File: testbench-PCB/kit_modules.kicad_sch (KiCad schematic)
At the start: 14 parts, among them U2 Rotary_encoder_switch_module, U3 Thermistor_module, U4 Relay_module, U6 Matrix_keyboard, U7 RTC_EEPROM_module, U8 LCD_display

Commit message: Updated footprints, PCB.
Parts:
- U2: footprint Connector_PinSocket_2.54mm:PinSocket_1x05_P2.54mm_Horizontal -> kit_modules:Encoder_module
- U4: footprint (none) -> kit_modules:Relay_module
- U7: footprint Connector_PinSocket_2.54mm:PinSocket_1x06_P2.54mm_Horizontal -> Connector_PinSocket_2.54mm:PinSocket_1x06_P2.54mm_Vertical
- U8: footprint (none) -> kit_modules:LCD_1602A_module
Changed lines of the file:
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@@
       (effects (font (size 1.27 1.27)))
     )
-    (property "Footprint" "" (at 177.8 54.61 0)
+    (property "Footprint" "kit_modules:Relay_module" (at 177.8 54.61 0)
       (effects (font (size 1.27 1.27)) hide)
     )
@@
       (effects (font (size 1.27 1.27)))
     )
-    (property "Footprint" "" (at 179.07 151.13 0)
+    (property "Footprint" "kit_modules:LCD_1602A_module" (at 179.07 151.13 0)
       (effects (font (size 1.27 1.27)) hide)
     )
@@
       (effects (font (size 1.27 1.27)))
     )
-    (property "Footprint" "Connector_PinSocket_2.54mm:PinSocket_1x05_P2.54mm_Horizontal" (at 87.63 50.8 0)
+    (property "Footprint" "kit_modules:Encoder_module" (at 87.63 50.8 0)
       (effects (font (size 1.27 1.27)) hide)
     )
@@
       (effects (font (size 1.27 1.27)))
     )
-    (property "Footprint" "Connector_PinSocket_2.54mm:PinSocket_1x06_P2.54mm_Horizontal" (at 90.17 177.8 0)
-      (effects (font (size 1.27 1.27)) hide)
-    )
+    (property "Footprint" "Connector_PinSocket_2.54mm:PinSocket_1x06_P2.54mm_Vertical" (at 90.17 177.8 0)
+      (effects (font (size 1.27 1.27)) hide)
+    )

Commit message: Routed osc., USB interface.
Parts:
- U3: footprint Connector_PinSocket_2.54mm:PinSocket_1x04_P2.54mm_Horizontal -> Connector_PinSocket_2.54mm:PinSocket_1x04_P2.54mm_Vertical
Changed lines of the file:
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@@
       (effects (font (size 1.27 1.27)))
     )
-    (property "Footprint" "Connector_PinSocket_2.54mm:PinSocket_1x04_P2.54mm_Horizontal" (at 210.82 95.25 0)
+    (property "Footprint" "Connector_PinSocket_2.54mm:PinSocket_1x04_P2.54mm_Vertical" (at 210.82 95.25 0)
       (effects (font (size 1.27 1.27)) hide)
     )

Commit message: Fixed footprints in schematics.
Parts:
- U2: footprint kit_modules:Encoder_module -> kit_modules:Rotary_encoder_module
- U3: footprint Connector_PinSocket_2.54mm:PinSocket_1x04_P2.54mm_Vertical -> kit_modules:Thermistor_module
- U7: footprint Connector_PinSocket_2.54mm:PinSocket_1x06_P2.54mm_Vertical -> kit_modules:RTC_module
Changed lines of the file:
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@@
       (effects (font (size 1.27 1.27)))
     )
-    (property "Footprint" "Connector_PinSocket_2.54mm:PinSocket_1x04_P2.54mm_Vertical" (at 210.82 95.25 0)
+    (property "Footprint" "kit_modules:Thermistor_module" (at 210.82 95.25 0)
       (effects (font (size 1.27 1.27)) hide)
     )
@@
       (effects (font (size 1.27 1.27)))
     )
-    (property "Footprint" "kit_modules:Encoder_module" (at 87.63 50.8 0)
+    (property "Footprint" "kit_modules:Rotary_encoder_module" (at 87.63 50.8 0)
       (effects (font (size 1.27 1.27)) hide)
     )
@@
       (effects (font (size 1.27 1.27)))
     )
-    (property "Footprint" "Connector_PinSocket_2.54mm:PinSocket_1x06_P2.54mm_Vertical" (at 90.17 177.8 0)
+    (property "Footprint" "kit_modules:RTC_module" (at 90.17 177.8 0)
       (effects (font (size 1.27 1.27)) hide)
     )

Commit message: Routing the PCB.
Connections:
- net +5V: now also U8.19 (5V); no longer U8.8 (5V)
- net GND: now also U8.20 (GND), U8.21 (GND); no longer U8.9 (GND)
- net LCD_AO: now also U8.23 (A0); no longer U8.10 (A0)
- net LCD_D0: now reaches U8.5 (D4)
- net LCD_D1: now reaches U8.6 (D5)
- net LCD_D2: now reaches U8.7 (D6)
- net KEY_D0: now reaches U6.1 (ROW1)
- net KEY_D1: now reaches U6.2 (ROW2)
- net KEY_D2: now reaches U6.3 (ROW3)
- net KEY_D3: now reaches U6.4 (ROW4)
- net KEY_D4: now reaches U6.5 (COL1)
- net KEY_D5: now reaches U6.6 (COL2)
- net KEY_D6: now reaches U6.7 (COL3)
- net KEY_D7: now reaches U6.8 (COL4)
- net A renamed ENC.A
- net B renamed ENC.B
- net SW renamed ENC.SW
- new net LCD_D3: U8.8 (D7)
- new net LCD_D4: U8.9 (RS)
- new net LCD_D5: U8.10 (E)
- new net LCD_D6: U8.17 (RST)

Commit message: Finished PCB routing, added ground plane.
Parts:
- C10: value C -> 1uF; footprint (none) -> Capacitor_SMD:C_0805_2012Metric
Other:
- moved on the sheet: U6
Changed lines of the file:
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@@
     (stroke (width 0) (type default))
   )
-  (bus_entry (at 81.28 105.41) (size 2.54 -2.54)
+  (bus_entry (at 82.55 105.41) (size 2.54 -2.54)
     (stroke (width 0) (type default))
   )
@@
     (stroke (width 0) (type default))
   )
-  (bus_entry (at 96.52 105.41) (size 2.54 -2.54)
+  (bus_entry (at 97.79 105.41) (size 2.54 -2.54)
     (stroke (width 0) (type default))
   )
@@
     (stroke (width 0) (type default))
   )
-  (bus_entry (at 88.9 105.41) (size 2.54 -2.54)
+  (bus_entry (at 90.17 105.41) (size 2.54 -2.54)
     (stroke (width 0) (type default))
   )
@@
     (stroke (width 0) (type default))
   )
-  (bus_entry (at 83.82 105.41) (size 2.54 -2.54)
+  (bus_entry (at 85.09 105.41) (size 2.54 -2.54)
     (stroke (width 0) (type default))
   )
@@
     (stroke (width 0) (type default))
   )
-  (bus_entry (at 86.36 105.41) (size 2.54 -2.54)
+  (bus_entry (at 87.63 105.41) (size 2.54 -2.54)
     (stroke (width 0) (type default))
   )
@@
     (stroke (width 0) (type default))
   )
-  (bus_entry (at 93.98 105.41) (size 2.54 -2.54)
-    (stroke (width 0) (type default))
-  )
-  (bus_entry (at 91.44 105.41) (size 2.54 -2.54)
+  (bus_entry (at 95.25 105.41) (size 2.54 -2.54)
+    (stroke (width 0) (type default))
+  )
+  (bus_entry (at 92.71 105.41) (size 2.54 -2.54)
     (stroke (width 0) (type default))
   )
@@
     (stroke (width 0) (type default))
   )
-  (bus_entry (at 78.74 105.41) (size 2.54 -2.54)
+  (bus_entry (at 80.01 105.41) (size 2.54 -2.54)
     (stroke (width 0) (type default))
   )
@@
     (stroke (width 0) (type default))
   )
-  (bus (pts (xy 62.23 105.41) (xy 78.74 105.41))
+  (bus (pts (xy 62.23 105.41) (xy 80.01 105.41))
     (stroke (width 0) (type default))
   )
@@
     (stroke (width 0) (type default))
   )
-  (wire (pts (xy 81.28 92.075) (xy 81.28 102.87))
+  (wire (pts (xy 82.55 92.71) (xy 82.55 102.87))
     (stroke (width 0) (type default))
   )
@@
     (stroke (width 0) (type default))
   )
-  (bus (pts (xy 78.74 105.41) (xy 81.28 105.41))
-    (stroke (width 0) (type default))
-  )
-  (wire (pts (xy 86.36 92.075) (xy 86.36 102.87))
+  (bus (pts (xy 80.01 105.41) (xy 82.55 105.41))
+    (stroke (width 0) (type default))
+  )
+  (wire (pts (xy 87.63 92.71) (xy 87.63 102.87))
     (stroke (width 0) (type default))
   )
@@
     (stroke (width 0) (type default))
   )
-  (wire (pts (xy 88.9 92.075) (xy 88.9 102.87))
+  (wire (pts (xy 90.17 92.71) (xy 90.17 102.87))
     (stroke (width 0) (type default))
   )
@@
     (stroke (width 0) (type default))
   )
-  (bus (pts (xy 83.82 105.41) (xy 86.36 105.41))
+  (bus (pts (xy 85.09 105.41) (xy 87.63 105.41))
     (stroke (width 0) (type default))
   )
@@
     (stroke (width 0) (type default))
   )
-  (wire (pts (xy 96.52 92.075) (xy 96.52 102.87))
+  (wire (pts (xy 97.79 92.71) (xy 97.79 102.87))
     (stroke (width 0) (type default))
   )
@@
     (stroke (width 0) (type default))
   )
-  (bus (pts (xy 86.36 105.41) (xy 88.9 105.41))
+  (bus (pts (xy 87.63 105.41) (xy 90.17 105.41))
     (stroke (width 0) (type default))
   )
@@
     (stroke (width 0) (type default))
   )
-  (wire (pts (xy 83.82 92.075) (xy 83.82 102.87))
+  (wire (pts (xy 85.09 92.71) (xy 85.09 102.87))
     (stroke (width 0) (type default))
   )
@@
     (stroke (width 0) (type default))
   )
-  (wire (pts (xy 99.06 92.075) (xy 99.06 102.87))
+  (wire (pts (xy 100.33 92.71) (xy 100.33 102.87))
     (stroke (width 0) (type default))
   )
@@
     (stroke (width 0) (type default))
   )
-  (wire (pts (xy 91.44 92.075) (xy 91.44 102.87))
-    (stroke (width 0) (type default))
-  )
-  (bus (pts (xy 91.44 105.41) (xy 93.98 105.41))
+  (wire (pts (xy 92.71 92.71) (xy 92.71 102.87))
+    (stroke (width 0) (type default))
+  )
+  (bus (pts (xy 92.71 105.41) (xy 95.25 105.41))
     (stroke (width 0) (type default))
   )
@@
     (stroke (width 0) (type default))
   )
-  (wire (pts (xy 93.98 92.075) (xy 93.98 102.87))
+  (wire (pts (xy 95.25 92.71) (xy 95.25 102.87))
     (stroke (width 0) (type default))
   )
@@
     (stroke (width 0) (type default))
   )
-  (bus (pts (xy 88.9 105.41) (xy 91.44 105.41))
-    (stroke (width 0) (type default))
-  )
-  (bus (pts (xy 81.28 105.41) (xy 83.82 105.41))
-    (stroke (width 0) (type default))
-  )
-  (bus (pts (xy 93.98 105.41) (xy 96.52 105.41))
+  (bus (pts (xy 90.17 105.41) (xy 92.71 105.41))
+    (stroke (width 0) (type default))
+  )
+  (bus (pts (xy 82.55 105.41) (xy 85.09 105.41))
+    (stroke (width 0) (type default))
+  )
+  (bus (pts (xy 95.25 105.41) (xy 97.79 105.41))
     (stroke (width 0) (type default))
   )
@@
     (effects (font (size 1.27 1.27)) (justify left bottom))
   )
-  (label "KEY_D3" (at 88.9 102.87 90) (fields_autoplaced)
-    (effects (font (size 1.27 1.27)) (justify left bottom))
-  )
-  (label "KEY_D0" (at 81.28 102.87 90) (fields_autoplaced)
+  (label "KEY_D3" (at 90.17 102.87 90) (fields_autoplaced)
+    (effects (font (size 1.27 1.27)) (justify left bottom))
+  )
+  (label "KEY_D0" (at 82.55 102.87 90) (fields_autoplaced)
     (effects (font (size 1.27 1.27)) (justify left bottom))
   )
@@
     (effects (font (size 1.27 1.27)) (justify left bottom))
   )
-  (label "KEY_D2" (at 86.36 102.87 90) (fields_autoplaced)
+  (label "KEY_D2" (at 87.63 102.87 90) (fields_autoplaced)
     (effects (font (size 1.27 1.27)) (justify left bottom))
   )
@@
     (effects (font (size 1.27 1.27)) (justify left bottom))
   )
-  (label "KEY_D1" (at 83.82 102.87 90) (fields_autoplaced)
+  (label "KEY_D1" (at 85.09 102.87 90) (fields_autoplaced)
     (effects (font (size 1.27 1.27)) (justify left bottom))
   )
@@
     (effects (font (size 1.27 1.27)) (justify right bottom))
   )
-  (label "KEY_D5" (at 93.98 102.87 90) (fields_autoplaced)
-    (effects (font (size 1.27 1.27)) (justify left bottom))
-  )
-  (label "KEY_D4" (at 91.44 102.87 90) (fields_autoplaced)
+  (label "KEY_D5" (at 95.25 102.87 90) (fields_autoplaced)
+    (effects (font (size 1.27 1.27)) (justify left bottom))
+  )
+  (label "KEY_D4" (at 92.71 102.87 90) (fields_autoplaced)
     (effects (font (size 1.27 1.27)) (justify left bottom))
   )
@@
     (effects (font (size 1.27 1.27)) (justify left bottom))
   )
-  (label "KEY_D6" (at 96.52 102.87 90) (fields_autoplaced)
-    (effects (font (size 1.27 1.27)) (justify left bottom))
-  )
-  (label "KEY_D7" (at 99.06 102.87 90) (fields_autoplaced)
+  (label "KEY_D6" (at 97.79 102.87 90) (fields_autoplaced)
+    (effects (font (size 1.27 1.27)) (justify left bottom))
+  )
+  (label "KEY_D7" (at 100.33 102.87 90) (fields_autoplaced)
     (effects (font (size 1.27 1.27)) (justify left bottom))
   )
@@
       (effects (font (size 1.27 1.27)))
     )
-    (property "Value" "C" (at 78.74 123.19 90)
-      (effects (font (size 1.27 1.27)))
-    )
-    (property "Footprint" "" (at 82.55 127.3048 0)
+    (property "Value" "1uF" (at 78.74 123.19 90)
+      (effects (font (size 1.27 1.27)))
+    )
+    (property "Footprint" "Capacitor_SMD:C_0805_2012Metric" (at 82.55 127.3048 0)
       (effects (font (size 1.27 1.27)) hide)
     )
@@
     )
   )
-  (symbol (lib_id "kit_modules:matrix_keyboard") (at 78.74 89.535 0) (unit 1)
+  (symbol (lib_id "kit_modules:matrix_keyboard") (at 80.01 90.17 0) (unit 1)
     (in_bom yes) (on_board yes) (dnp no)
-    (property "Reference" "U6" (at 102.87 81.28 0)
+    (property "Reference" "U6" (at 104.14 81.915 0)
       (effects (font (size 1.27 1.27)) (justify left))
     )
-    (property "Value" "Matrix_keyboard" (at 86.36 71.755 0)
-      (effects (font (size 1.27 1.27)))
-    )
-    (property "Footprint" "Connector_PinSocket_2.54mm:PinSocket_1x08_P2.54mm_Vertical" (at 78.74 89.535 0)
-      (effects (font (size 1.27 1.27)) hide)
-    )
-    (property "Datasheet" "" (at 78.74 89.535 0)
-      (effects (font (size 1.27 1.27)) hide)
-    )
+    (property "Value" "Matrix_keyboard" (at 87.63 72.39 0)
+      (effects (font (size 1.27 1.27)))
+    )
+    (property "Footprint" "Connector_PinSocket_2.54mm:PinSocket_1x08_P2.54mm_Vertical" (at 80.01 90.17 0)
+      (effects (font (size 1.27 1.27)) hide)
+    )
+    (property "Datasheet" "" (at 80.01 90.17 0)
+      (effects (font (size 1.27 1.27)) hide)
+    )

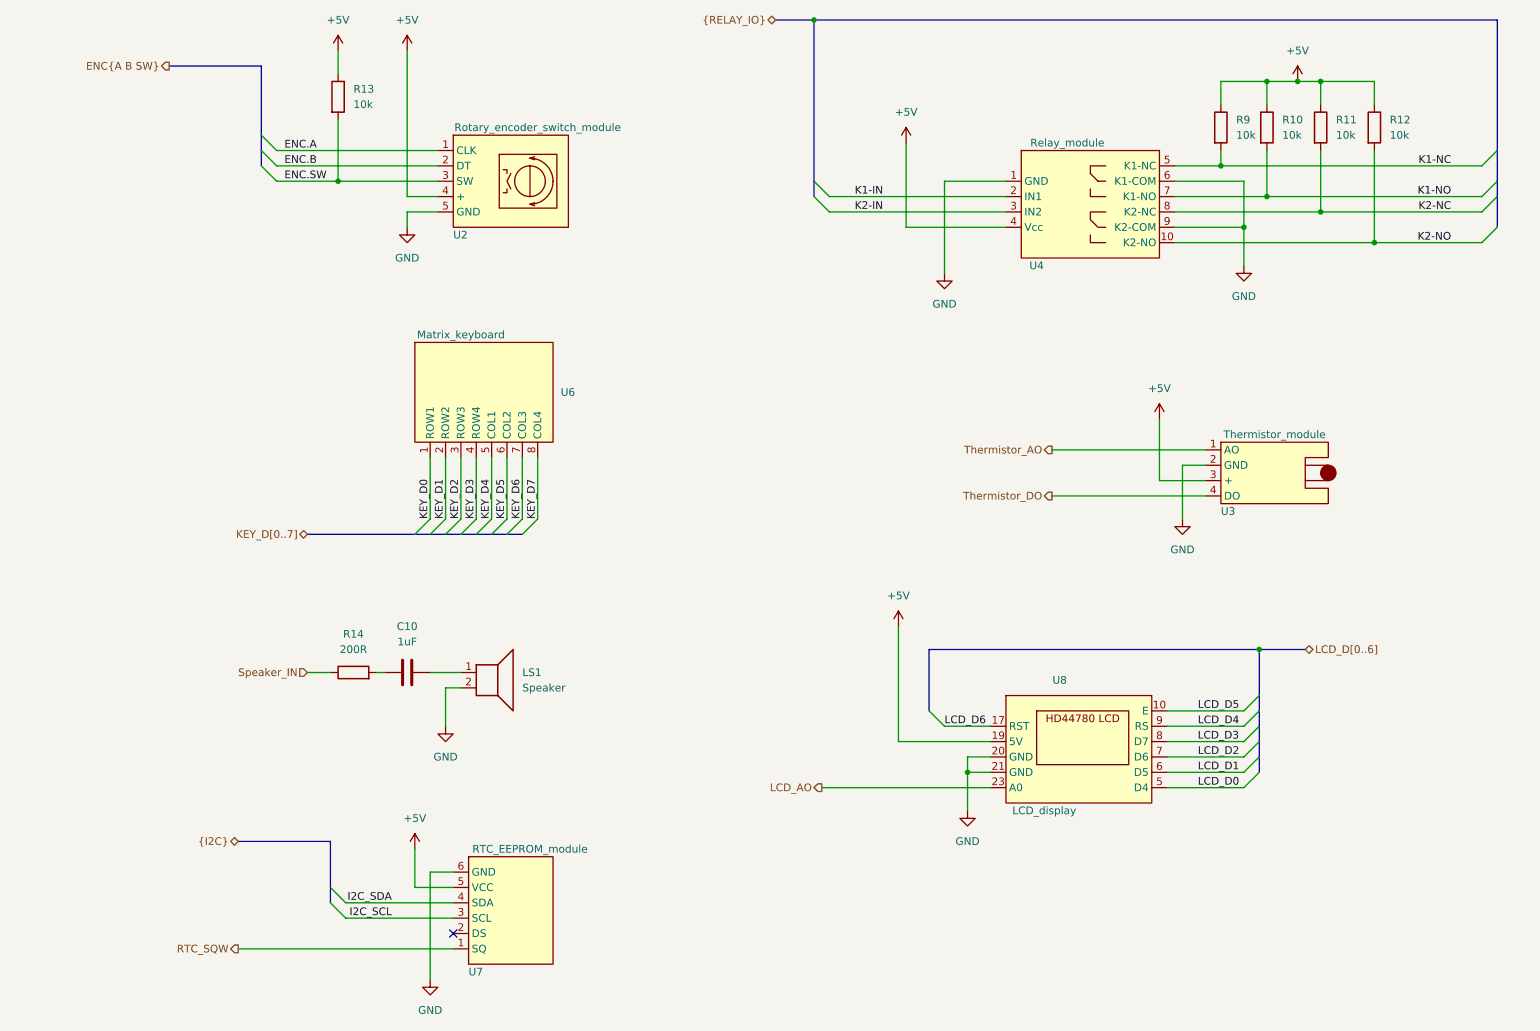
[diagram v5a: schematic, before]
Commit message: Added protective resistors.
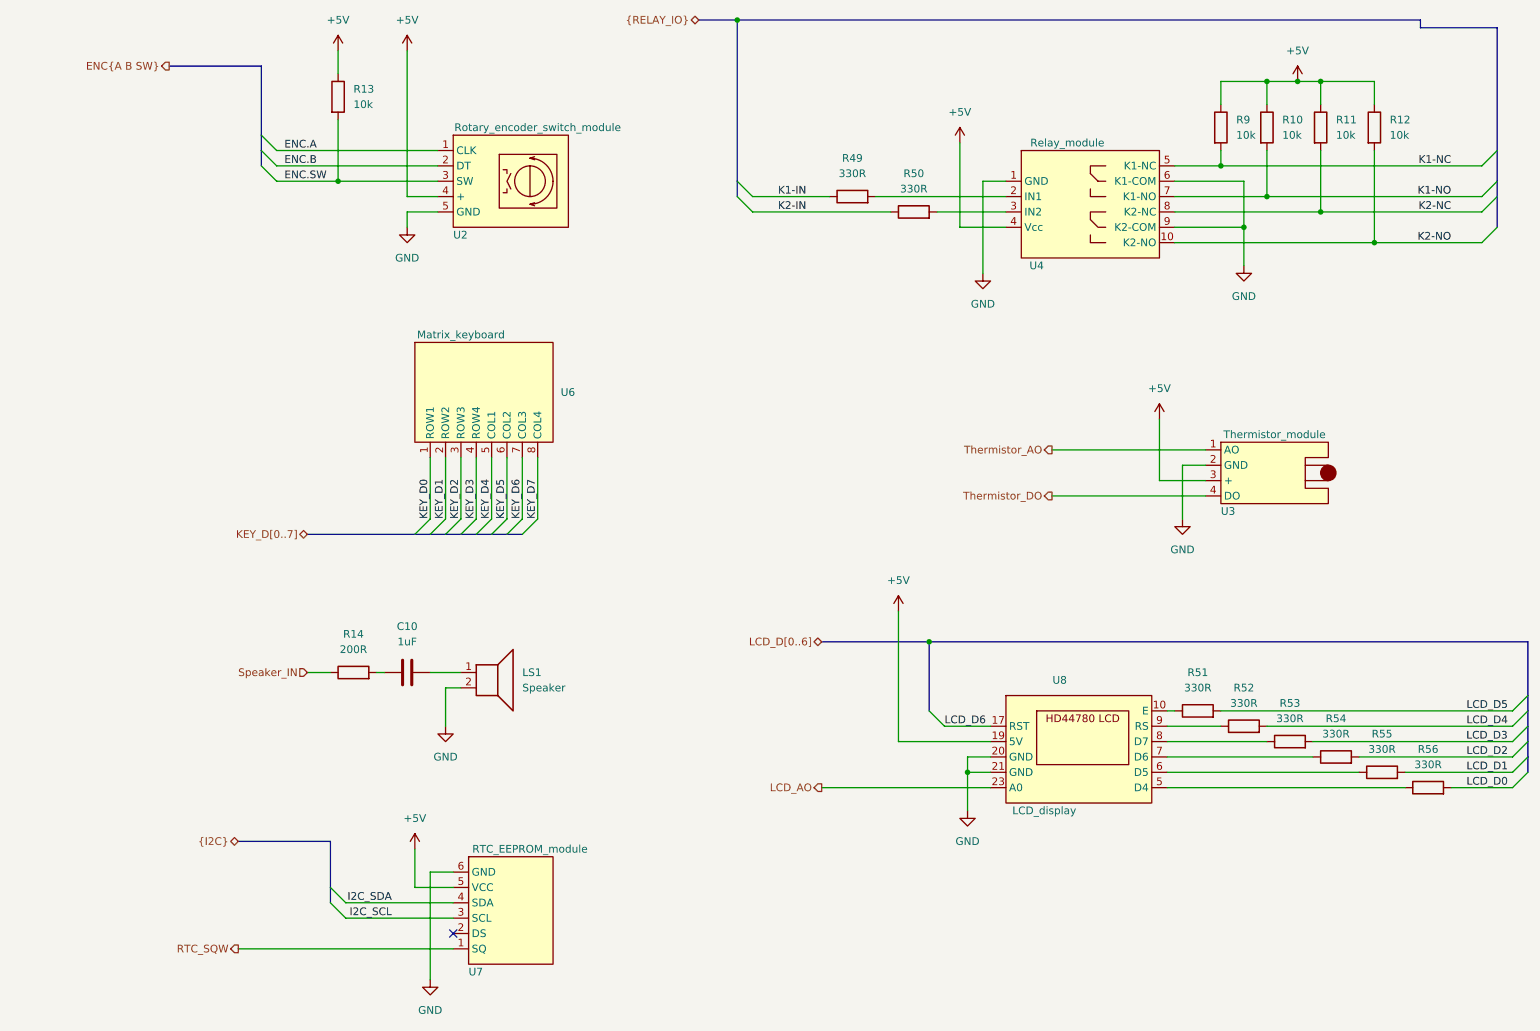
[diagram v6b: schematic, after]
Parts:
- added R49, R50, R51, R52, R53, R54, R55, R56: 330R, Resistor_SMD:R_0805_2012Metric, symbol Device:R
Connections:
- net K1-IN: now also R49.1; no longer U4.2 (IN1)
- net K2-IN: now also R50.1; no longer U4.3 (IN2)
- net LCD_D0: now also R56.2; no longer U8.5 (D4)
- net LCD_D1: now also R55.2; no longer U8.6 (D5)
- net LCD_D2: now also R54.2; no longer U8.7 (D6)
- net LCD_D3: now also R53.2; no longer U8.8 (D7)
- net LCD_D4: now also R52.2; no longer U8.9 (RS)
- net LCD_D5: now also R51.2; no longer U8.10 (E)
- new net: R49.2, U4.2 (IN1)
- new net: R50.2, U4.3 (IN2)
- new net: R51.1, U8.10 (E)
- new net: R56.1, U8.5 (D4)
- new net: R55.1, U8.6 (D5)
- new net: R54.1, U8.7 (D6)
- new net: R53.1, U8.8 (D7)
- new net: R52.1, U8.9 (RS)
